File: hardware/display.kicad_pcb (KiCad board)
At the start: 2 copper layers, 18.8 x 27.9 mm, 14 parts, among them J1 Conn_02x06_Counter_Clockwise, J2 Conn_01x05_Female, J3 Conn_01x02_Female, SW1 SW_Push, U1 MDBT42Q

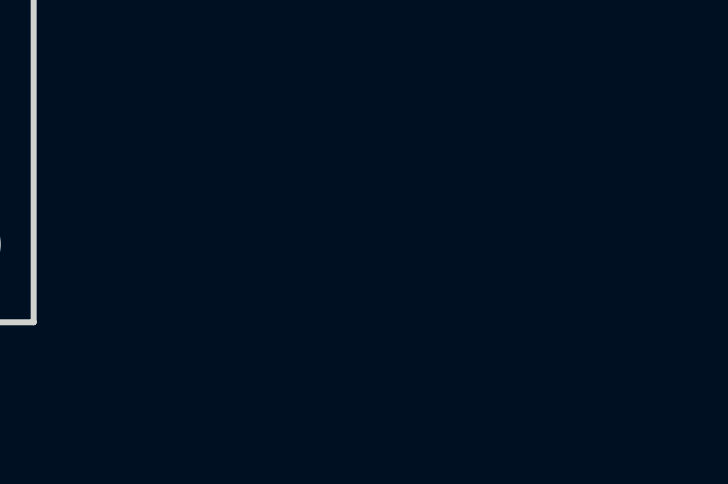
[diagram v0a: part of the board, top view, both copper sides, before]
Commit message: add i2c
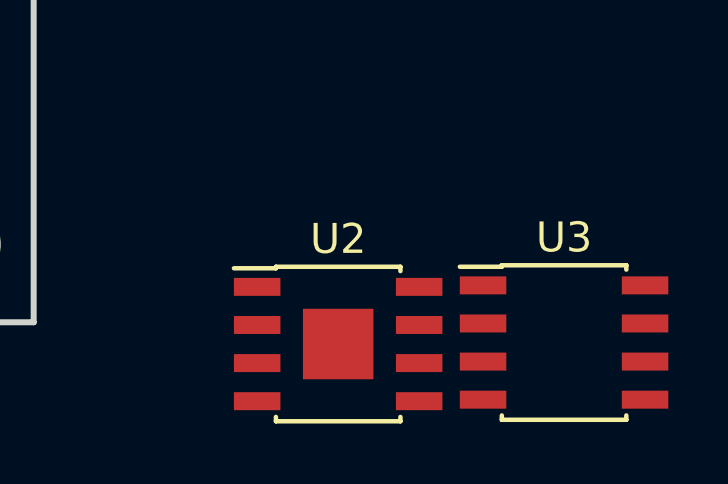
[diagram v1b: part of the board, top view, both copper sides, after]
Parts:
- added U2: AS5601, Package_SO:SOIC-8-1EP_3.9x4.9mm_P1.27mm_EP2.35x2.35mm, F.Cu at (127.8, 106.0)
- added U3: DS3231MZ, Package_SO:SOIC-8_3.9x4.9mm_P1.27mm, F.Cu at (135.3, 106.0)
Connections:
- U1 pad 10: (no net) -> Net-(U1-Pad10)
- U1 pad 14: (no net) -> Net-(U1-Pad14)
- U1 pad 15: (no net) -> Net-(U1-Pad15)
- U1 pad 16: (no net) -> Net-(U1-Pad16)
- U1 pad 17: (no net) -> Net-(U1-Pad17)
- U1 pad 18: (no net) -> Net-(U1-Pad18)
- U1 pad 19: (no net) -> Net-(U1-Pad19)
- U1 pad 2: (no net) -> Net-(U1-Pad2)
- U1 pad 20: (no net) -> Net-(U1-Pad20)
- U1 pad 21: (no net) -> Net-(U1-Pad21)
- U1 pad 22: (no net) -> Net-(U1-Pad22)
- U1 pad 23: (no net) -> Net-(U1-Pad23)
- U1 pad 25: (no net) -> /i2c_subsystem/SCL
- U1 pad 26: (no net) -> /i2c_subsystem/SDA
- U1 pad 27: (no net) -> Net-(U1-Pad27)
- U1 pad 28: (no net) -> Net-(U1-Pad28)
- U1 pad 38: (no net) -> Net-(U1-Pad38)
- U1 pad 40: (no net) -> Net-(U1-Pad40)
- U1 pad 41: (no net) -> Net-(U1-Pad41)
- U1 pad 9: (no net) -> Net-(U1-Pad9)
